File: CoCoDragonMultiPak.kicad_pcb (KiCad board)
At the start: 2 copper layers, 148.6 x 175.4 mm, 58 parts, among them IC1 74LS245DWR, IC10 74LS74ADR, IC11 74LS153DR, IC12 74ALS30ADR, IC13 GAL16V8, IC2 74LS367ADR, IC3 74LS367ADR, IC4 74LS367ADR, IC5 74LS367ADR, IC6 74LS367ADR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

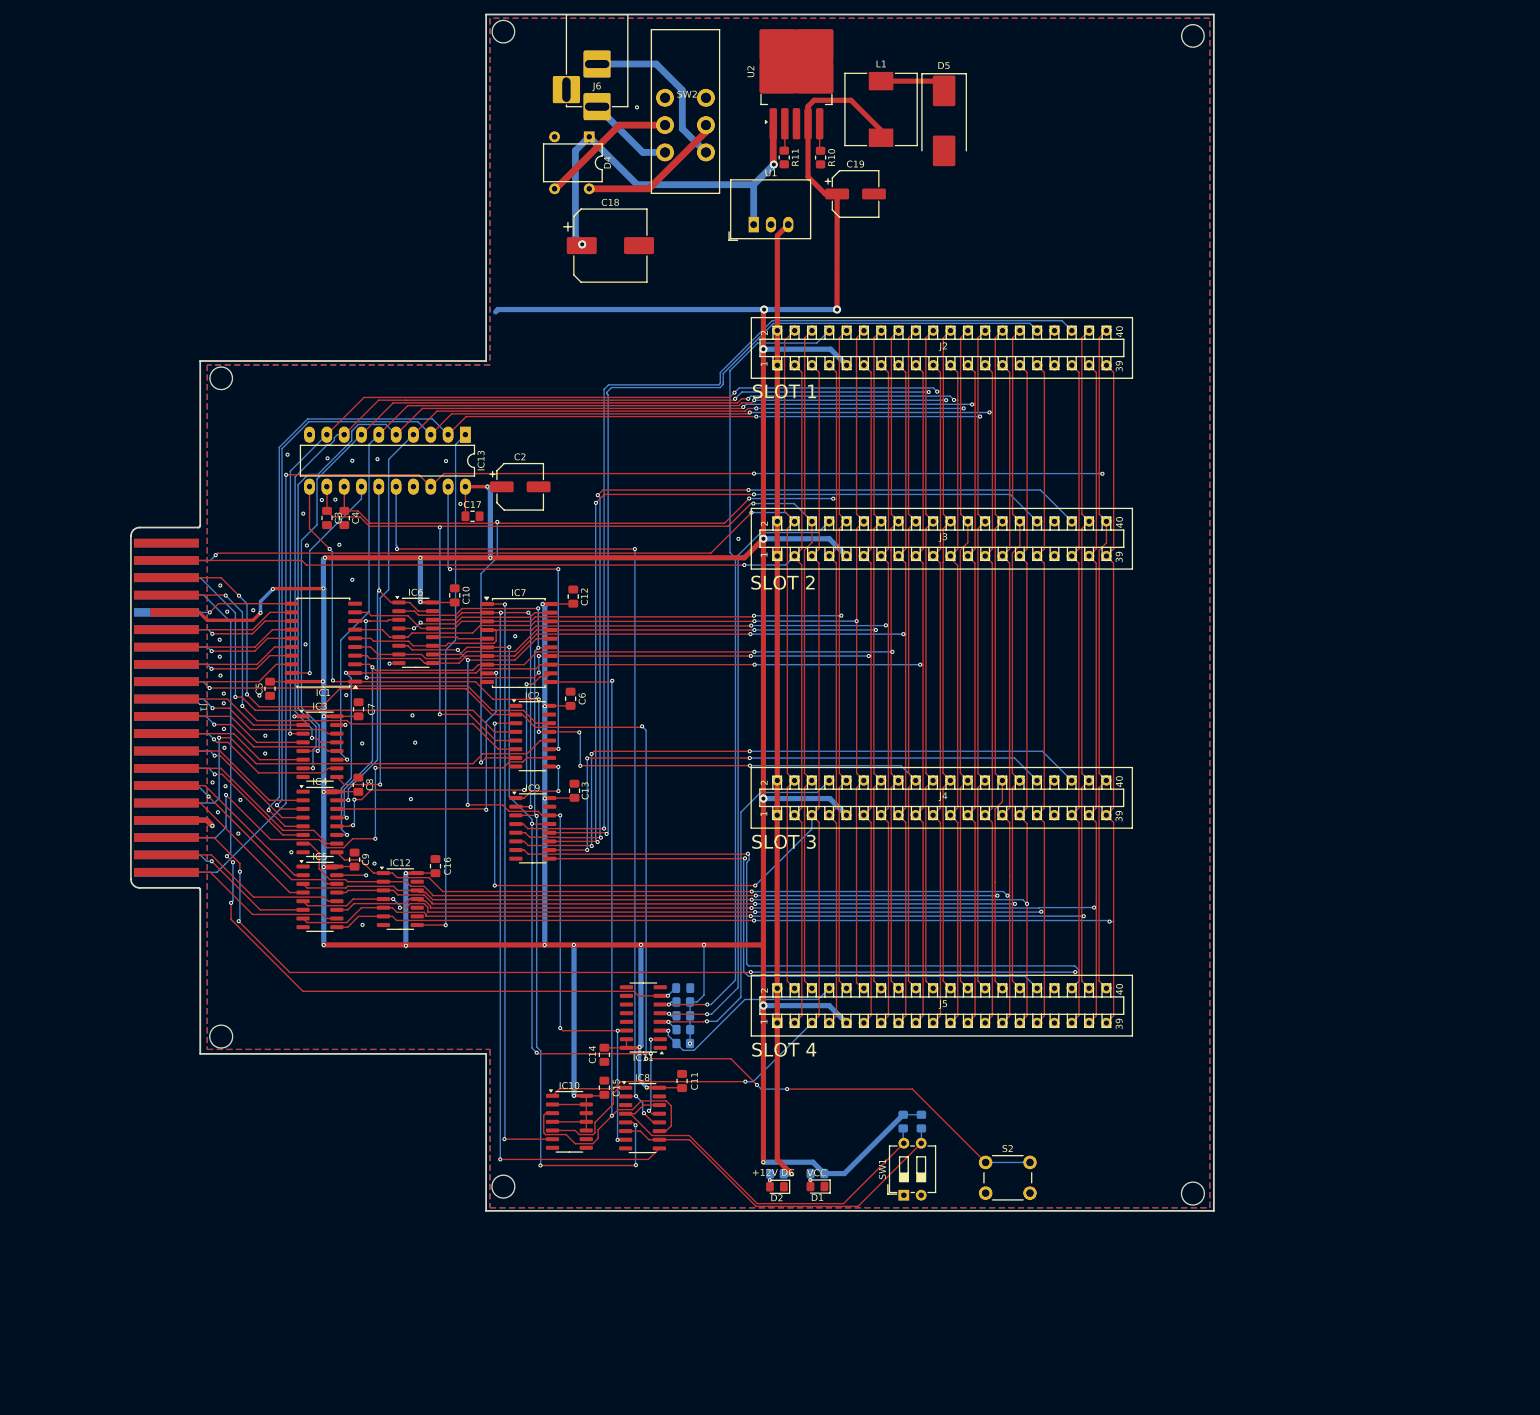
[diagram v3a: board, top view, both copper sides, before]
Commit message: refine power circuit layout
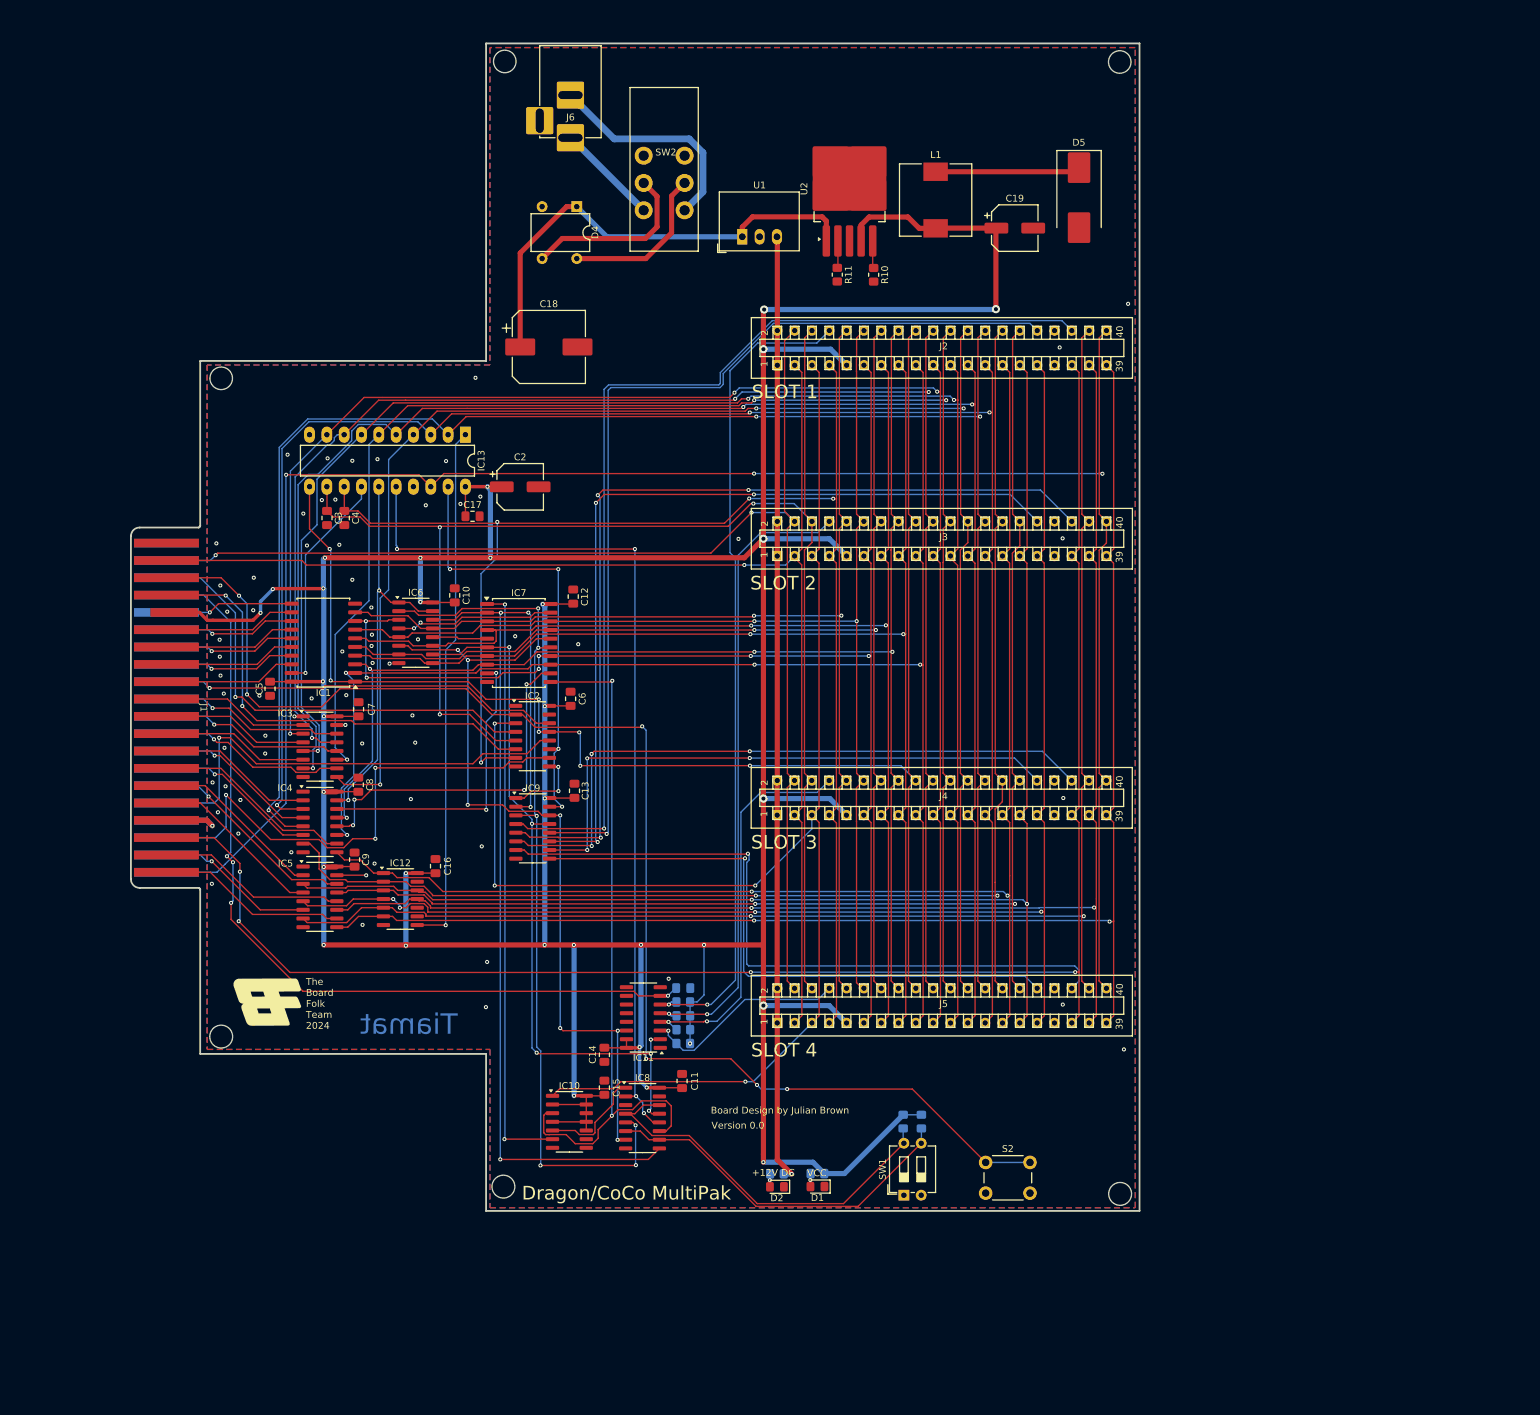
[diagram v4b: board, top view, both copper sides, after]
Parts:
- added Ge: LOGO, PowerBoard:BoardFolk, F.Cu at (70.9, 195.1)
- moved C19 23.9 mm to (180.1, 75.6)
- moved D5 22.8 mm to (189.5, 71.1)
- moved R10 18.9 mm to (159.4, 82.5)
- moved R11 18.9 mm to (154.1, 82.4)
- moved U2 18.9 mm to (155.9, 69.8)
- moved C18 17.4 mm to (111.8, 93.0)
- moved L1 15.5 mm to (168.5, 71.5)
- moved D4 10.4 mm to (115.9, 72.5)
- moved SW2 9.04 mm to (128.9, 65.0)
- moved J6 6.00 mm to (115.0, 59.9)
- moved U1 2.44 mm to (140.2, 76.9)
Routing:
- net +5V: track 737.2 -> 709.7 mm
- net Net-(D5-K): track 9.84 -> 21.3 mm
- net /I~{CTS}: track 55.8 -> 66.9 mm, vias 3 -> 4
- net /RECTIFIED_POWER: track 60.2 -> 68.5 mm, vias 2 -> 0
- net /AC1: track 24.6 -> 32.5 mm
- net Net-(SW2B-B): track 20.1 -> 26.0 mm
- net /AC2: track 12.7 -> 15.1 mm
- net +12V: track 141.9 -> 139.6 mm
- net Net-(SW2A-B): track 21.6 -> 23.6 mm
- net /IA3: track 236.7 -> 237.3 mm
- net GND: vias 47 -> 67
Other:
- board size 148.6 x 175.4 mm -> 137.7 x 171.2 mm
- board text added: "Board Design by Julian Brown"
- board text added: "Dragon/CoCo MultiPak"
- board text added: "The Board Folk Team 2024"
- board text added: "Tiamat"
- board text added: "Version 0.0"

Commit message: revise layout
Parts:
- moved Ge 110.5 mm to (180.5, 209.5)
- moved C17 14.0 mm to (114.2, 114.6), turned to -90 degrees
- moved C2 12.3 mm to (119.6, 110.9), turned to 90 degrees
- moved C3 11.4 mm to (90.7, 118.1)
- moved C4 11.4 mm to (93.2, 118.1)
- moved IC13 11.4 mm to (111.0, 105.9)
- moved J3 4.17 mm to (169.7, 125.1)
- moved J4 1.68 mm to (169.7, 157.2)
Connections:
- J1 pad 9: +5V -> unconnected-(J1-Pin_9-Pad9)
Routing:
- net +5V: track 709.7 -> 680.4 mm, vias 33 -> 30
- net /IQ: track 218.7 -> 206.2 mm
- net /CTRL1: track 131.7 -> 120.4 mm
- net /I~{CTS}: track 66.9 -> 55.6 mm
- net /IE: track 217.3 -> 206.6 mm
- net /~{ENBUS}: track 32.7 -> 42.1 mm
- net /IA3: track 237.3 -> 230.6 mm
- net /IA6: track 263.8 -> 257.8 mm
- net /IA7: track 265.8 -> 259.9 mm
- net /IA1: track 241.0 -> 235.5 mm
- net /IA0: track 240.1 -> 234.6 mm
- net /IA4: track 249.6 -> 244.3 mm
- net /~{SLEN}: track 290.7 -> 285.4 mm
- net /IA2: track 242.4 -> 237.6 mm
- net /FFxx: track 77.3 -> 82.0 mm
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
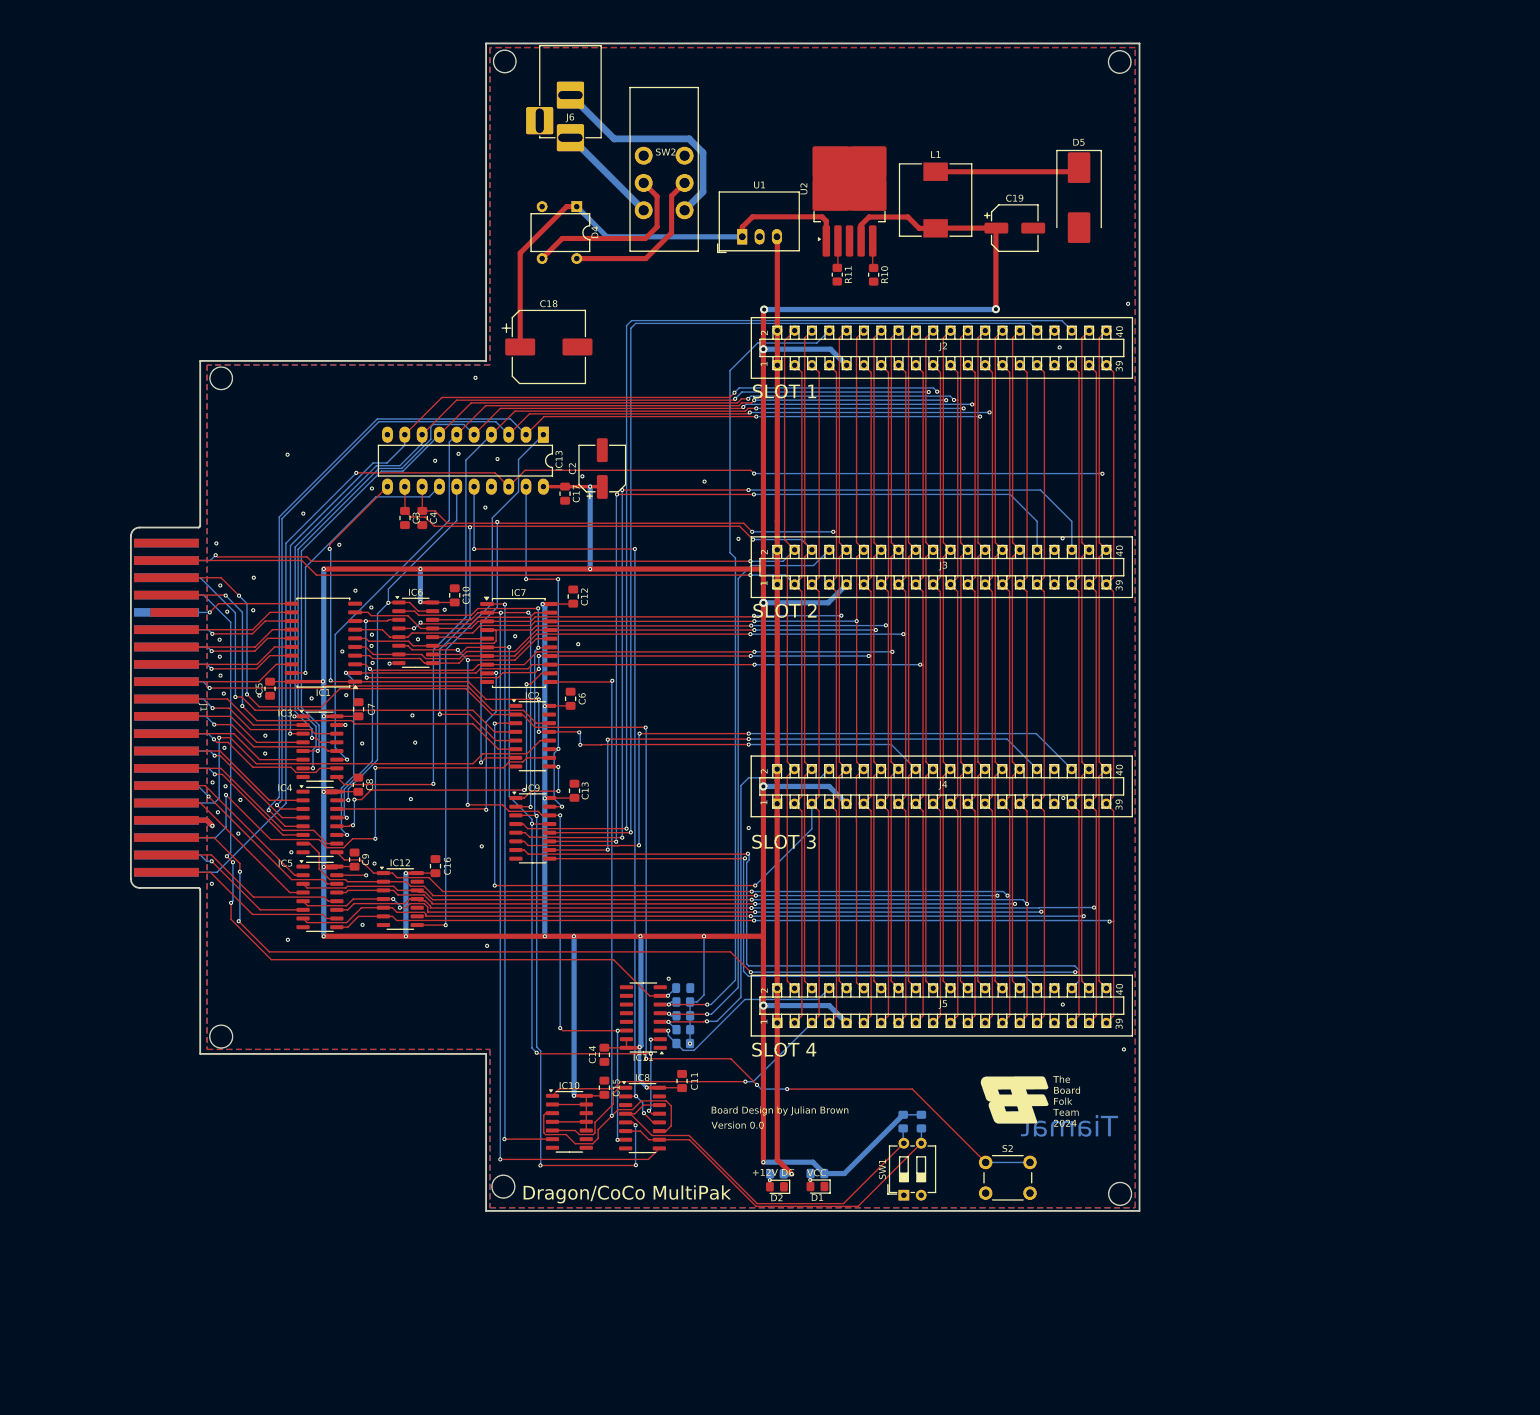
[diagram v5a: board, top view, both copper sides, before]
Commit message: populate supplier specific part numbers
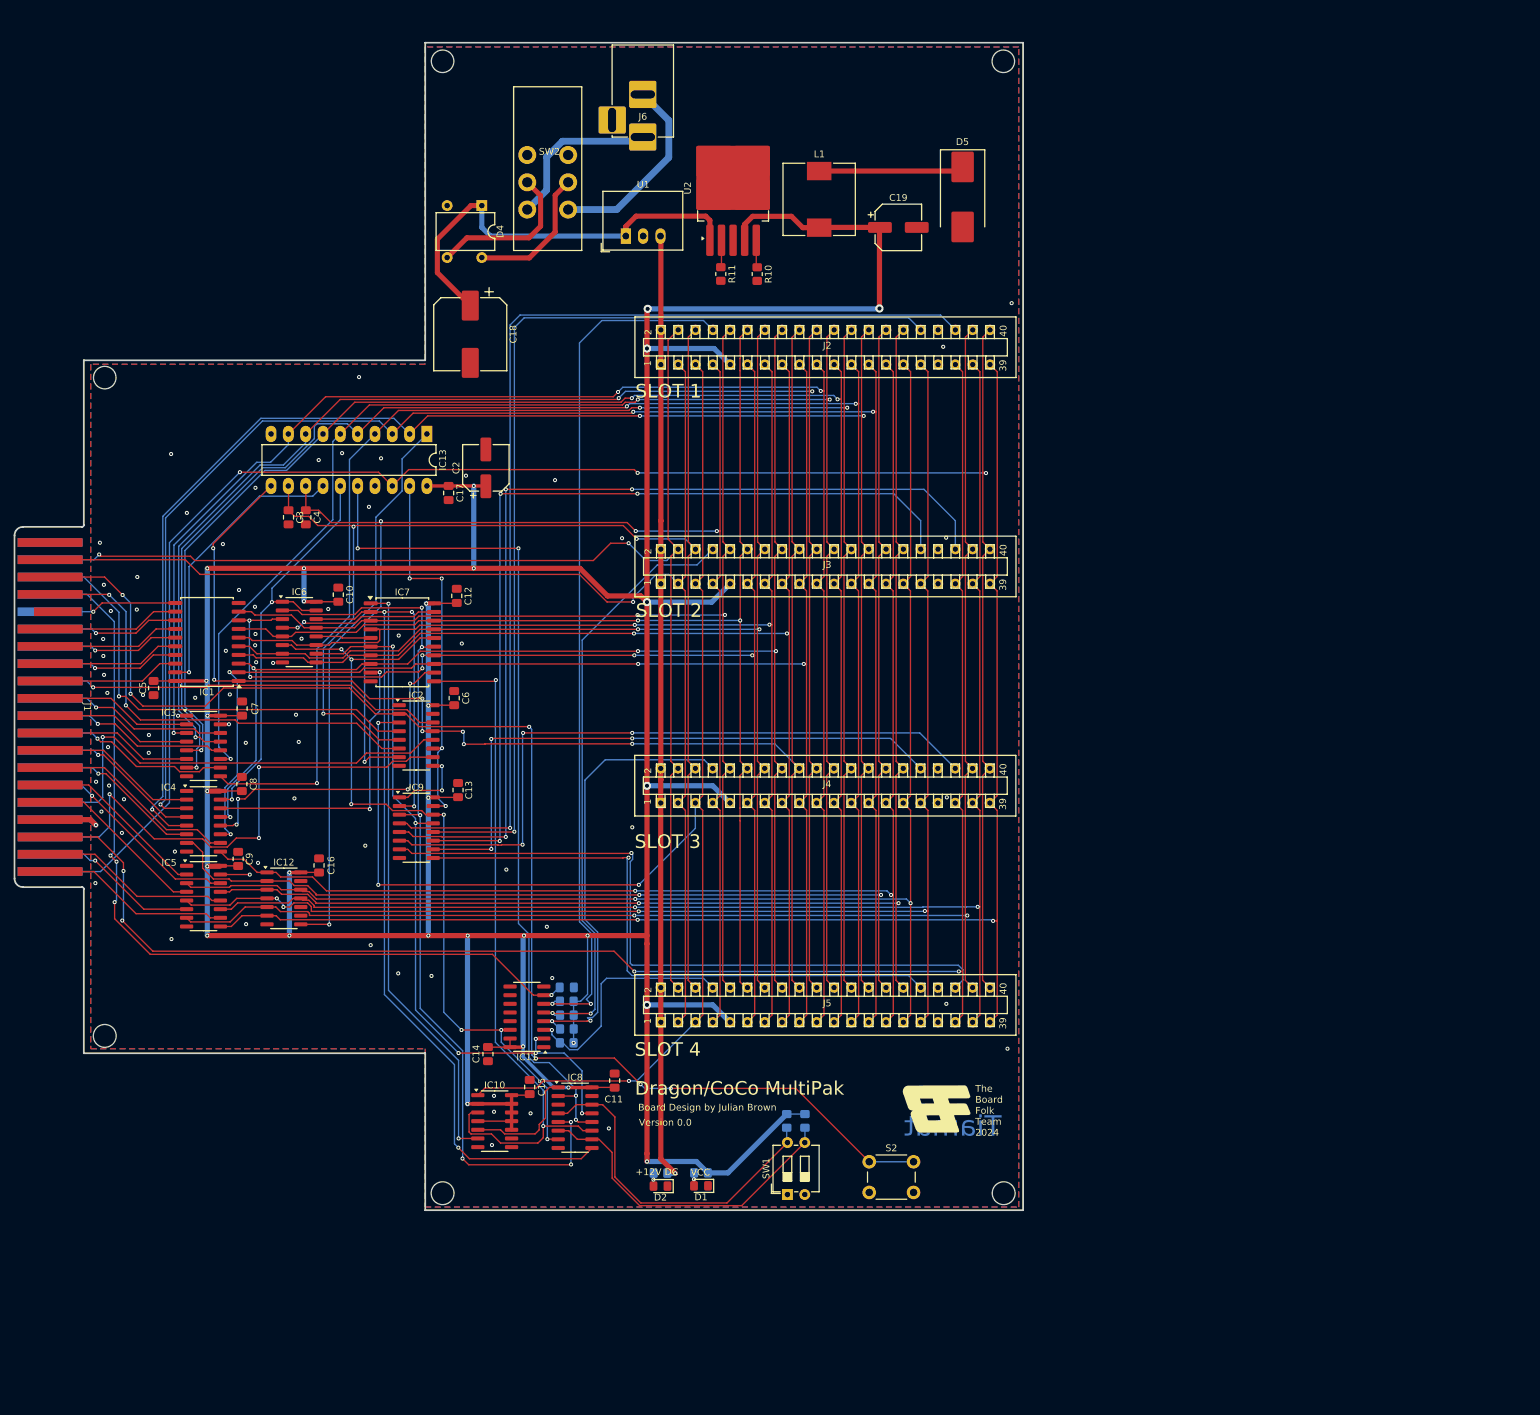
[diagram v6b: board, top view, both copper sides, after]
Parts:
- moved C3 17.1 mm to (73.6, 118.0)
- moved SW2 17.1 mm to (111.9, 64.9)
- moved C1 17.1 mm to (114.4, 186.9)
- moved C10 17.1 mm to (80.9, 129.4)
- moved C12 17.1 mm to (98.3, 129.5)
- moved C13 17.1 mm to (98.5, 158.0)
- moved C14 17.1 mm to (102.9, 196.7)
- moved C16 17.1 mm to (78.1, 169.1)
- moved C17 17.1 mm to (97.1, 114.5)
- moved C19 17.1 mm to (163.0, 75.5)
- moved C2 17.1 mm to (102.6, 110.8)
- moved C4 17.1 mm to (76.2, 118.0)
- moved C6 17.1 mm to (97.9, 144.5)
- moved C7 17.1 mm to (66.8, 146.1)
- moved C8 17.1 mm to (66.8, 157.1)
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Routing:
- net /AC2: track 15.1 -> 24.2 mm
- net +5V: track 680.4 -> 688.6 mm
- net /~{CART1}: track 120.5 -> 127.9 mm
- net /DEFAULT0: track 58.4 -> 51.2 mm
- net /~{CART3}: track 59.9 -> 66.3 mm
- net /I~{RESET}: track 222.0 -> 215.9 mm
- net /CTRL1: track 120.4 -> 126.4 mm
- net /RECTIFIED_POWER: track 68.5 -> 62.7 mm
- net /DEFAULT1: track 53.9 -> 48.9 mm
- net /~{CART4}: track 30.2 -> 34.9 mm
- net /REGS1: track 129.8 -> 134.2 mm
- net /AC1: track 32.5 -> 28.7 mm
- net /~{HALT}: track 192.6 -> 196.4 mm
- net /LOADREG: track 104.9 -> 101.4 mm
- net Net-(SW2B-B): track 26.0 -> 22.9 mm
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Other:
- outline, holes or cut-outs redrawn

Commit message: update to rev 0.2
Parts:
- removed R11: 47K, Resistor_SMD:R_0805_2012Metric_Pad1.20x1.40mm_HandSolder
- IC12: value 74ALS30ADR -> 74AHCT30D
- R10: value 47K -> 4K7
- moved D5 20.3 mm to (155.8, 59.5), turned to 0 degrees
- turned L1 to -90 degrees
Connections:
- L1 pad 1: +5V -> Net-(D5-K)
- L1 pad 2: Net-(D5-K) -> +5V
- U2 pad 2: Net-(U2-OUT) -> Net-(D5-K)
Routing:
- net Net-(D5-K): track 21.3 -> 77.6 mm
- net Net-(U2-OUT): track 3.98 -> 0.00 mm
- net +5V: track 688.6 -> 684.6 mm
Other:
- outline, holes or cut-outs redrawn
- board text added: "Version 0.1"
- board text removed: "Version 0.0"
